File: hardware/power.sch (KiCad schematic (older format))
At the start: 18 parts, among them J7 Barrel_Jack, U18 LT1529CQ#PBF, U19 LT1528CQ

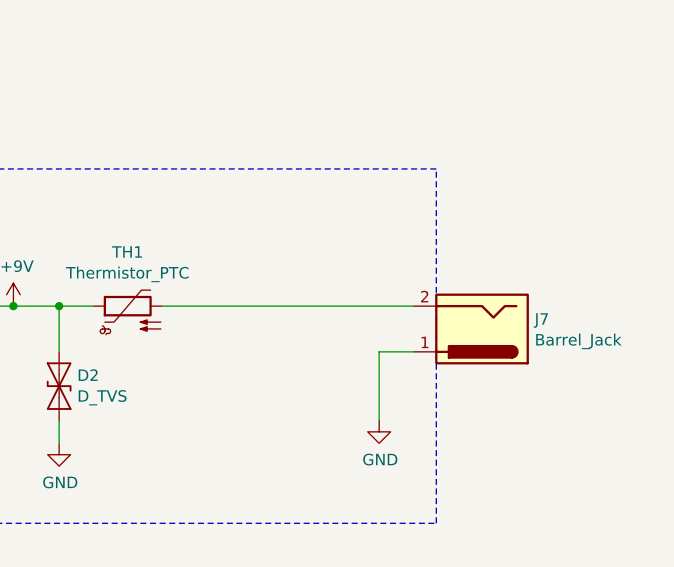
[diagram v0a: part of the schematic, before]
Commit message: update top overlay, drc przechodzi, dodny shielding wokół ścieżek zegarowych, dodane zdjęcia płytki
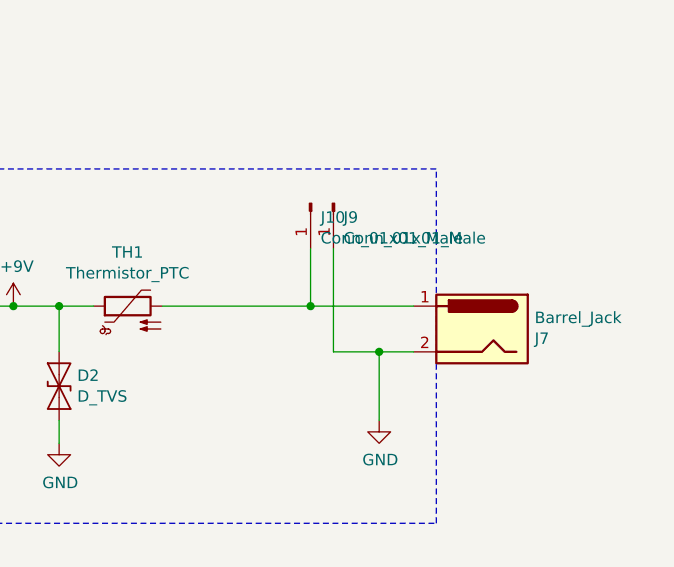
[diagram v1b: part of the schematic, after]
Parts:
- added J10, J9: Conn_01x01_Male, Connector_Wire:SolderWirePad_1x01_Drill2.5mm, symbol Connector:Conn_01x01_Male
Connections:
- net GND: now also J7.2, J9.1 (Pin_1); no longer J7.1
- net at TH1.2: now also J7.1, J10.1 (Pin_1); no longer J7.2
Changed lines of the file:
@@
 F 3 "~" H 10050 2010 50  0001 C CNN
 	1    10000 2050
-	-1   0    0    1
+	-1   0    0    -1
 $EndComp
 Wire Wire Line
@@
 	8150 1950 7950 1950
 Wire Wire Line
-	8600 1950 9700 1950
+	8600 1950 9250 1950
 Wire Wire Line
 	2650 4200 2650 4400
@@
 Wire Wire Line
 	7000 4250 7750 4250
+Wire Wire Line
+	9350 1700 9350 2150
+Wire Wire Line
+	9350 2150 9550 2150
+Connection ~ 9550 2150
+Wire Wire Line
+	9250 1700 9250 1950
+Connection ~ 9250 1950
+Wire Wire Line
+	9250 1950 9700 1950
+$Comp
+L Connector:Conn_01x01_Male J9
+U 1 1 5CF71EF7
+P 9350 1500
+F 0 "J9" V 9412 1544 50  0000 L CNN
+F 1 "Conn_01x01_Male" V 9503 1544 50  0000 L CNN
+F 2 "Connector_Wire:SolderWirePad_1x01_Drill2.5mm" H 9350 1500 50  0001 C CNN
+F 3 "~" H 9350 1500 50  0001 C CNN
+	1    9350 1500
+	0    1    1    0
+$EndComp
+$Comp
+L Connector:Conn_01x01_Male J10
+U 1 1 5CF74160
+P 9250 1500
+F 0 "J10" V 9312 1544 50  0000 L CNN
+F 1 "Conn_01x01_Male" V 9403 1544 50  0000 L CNN
+F 2 "Connector_Wire:SolderWirePad_1x01_Drill2.5mm" H 9250 1500 50  0001 C CNN
+F 3 "~" H 9250 1500 50  0001 C CNN
+	1    9250 1500
+	0    1    1    0
+$EndComp
 $EndSCHEMATC

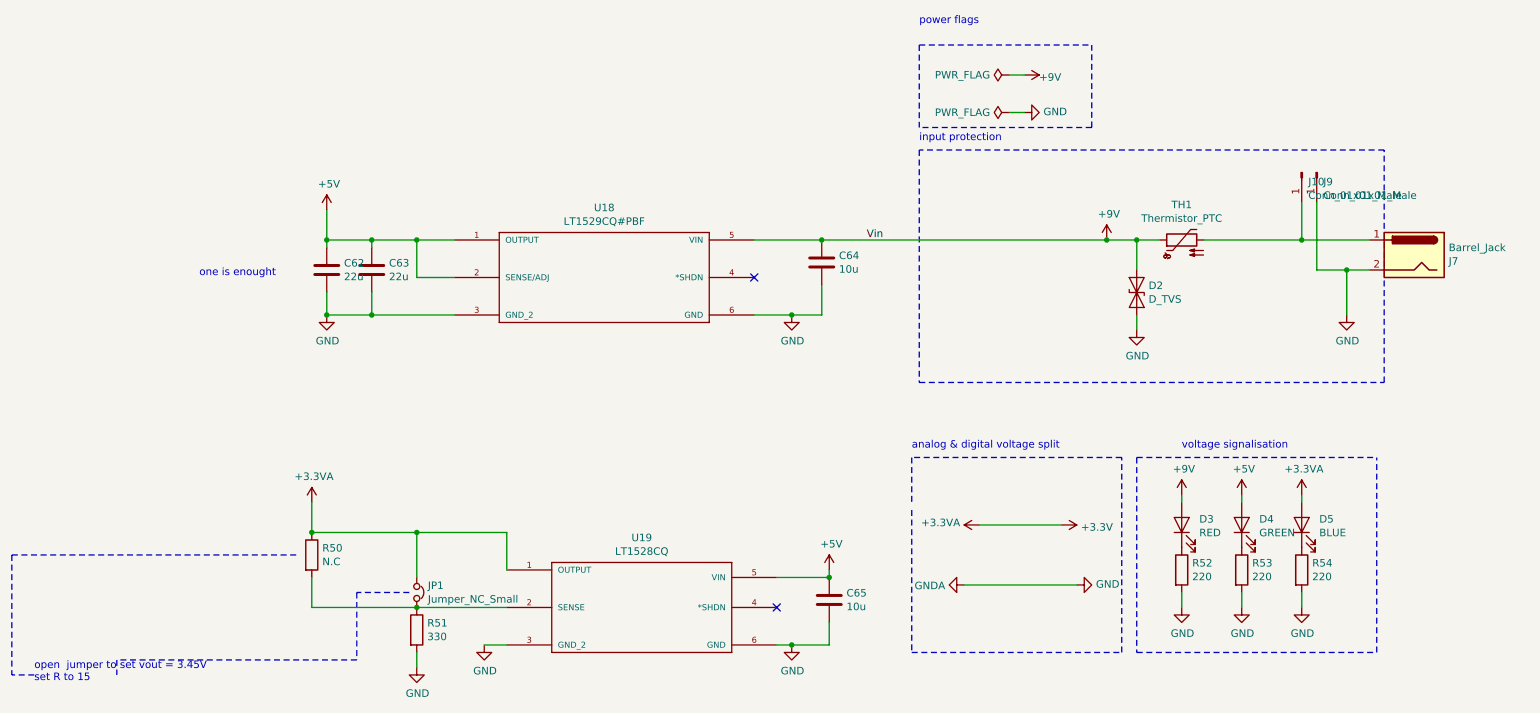
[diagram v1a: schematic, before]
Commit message: dodano poprawki błędów znalezionych podczas montażu
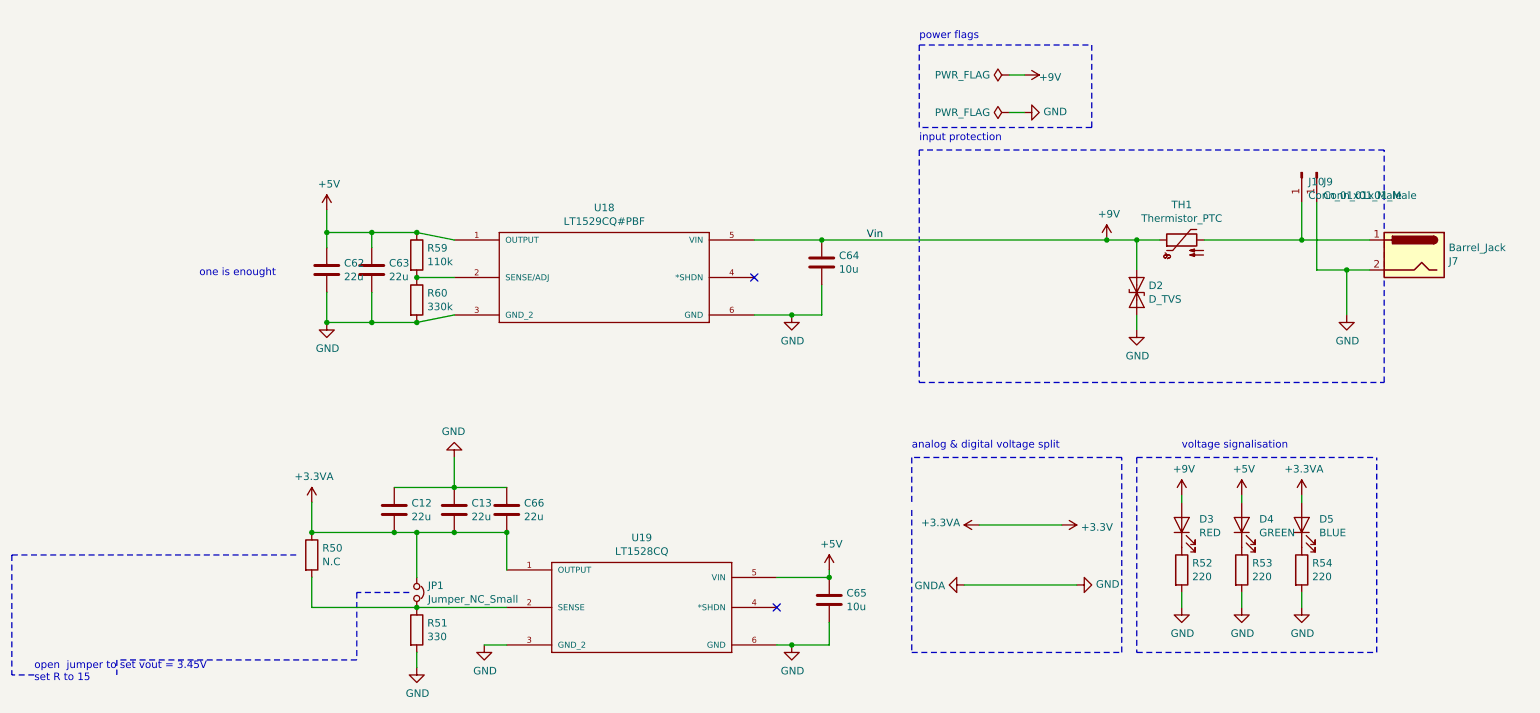
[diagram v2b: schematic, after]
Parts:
- added C12, C13, C66: 22u, Capacitor_SMD:C_0805_2012Metric_Pad1.15x1.40mm_HandSolder, symbol Device:C
- added R59: 110k, Resistor_SMD:R_0603_1608Metric_Pad1.05x0.95mm_HandSolder, symbol Device:R
- added R60: 330k, Resistor_SMD:R_0603_1608Metric_Pad1.05x0.95mm_HandSolder, symbol Device:R
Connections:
- net +3.3VA: now also C12.2, C13.2, C66.2
- net +5V: now also R59.1; no longer U18.2 (SENSE/ADJ)
- net GND: now also C12.1, C13.1, C66.1, R60.2
- new net: R59.2, R60.1, U18.2 (SENSE/ADJ)
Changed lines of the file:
@@
 	5850 4650 5750 4650
 Wire Wire Line
-	2650 4400 3350 4400
-Wire Wire Line
-	2650 3900 3350 3900
+	2650 3900 3200 3900
 Text Notes 800  4900 0    50   ~ 0
 open  jumper to set vout = 3.45V\nset R to 15
@@
 L power:GND #PWR0139
 U 1 1 5CEC8225
-P 2750 2450
-F 0 "#PWR0139" H 2750 2200 50  0001 C CNN
-F 1 "GND" H 2755 2277 50  0000 C CNN
-F 2 "" H 2750 2450 50  0001 C CNN
-F 3 "" H 2750 2450 50  0001 C CNN
-	1    2750 2450
-	1    0    0    -1
-$EndComp
-Wire Wire Line
-	3600 1950 3350 1950
-Wire Wire Line
-	3350 1950 3350 2200
+P 2750 2500
+F 0 "#PWR0139" H 2750 2250 50  0001 C CNN
+F 1 "GND" H 2755 2327 50  0000 C CNN
+F 2 "" H 2750 2500 50  0001 C CNN
+F 3 "" H 2750 2500 50  0001 C CNN
+	1    2750 2500
+	1    0    0    -1
+$EndComp
 Wire Wire Line
 	3350 2200 3600 2200
-Connection ~ 3350 1950
 $Comp
 L Device:C C62
@@
 $EndComp
 Wire Wire Line
-	3350 1950 3050 1950
-Wire Wire Line
-	2750 1950 2750 2000
-Wire Wire Line
-	2750 2300 2750 2450
-Connection ~ 2750 2450
-Wire Wire Line
-	2750 2450 3050 2450
+	2750 1900 2750 2000
+Wire Wire Line
+	2750 2300 2750 2500
+Connection ~ 2750 2500
+Wire Wire Line
+	2750 2500 3050 2500
 Wire Notes Line
 	3300 4300 2950 4300
@@
 $EndComp
 Wire Wire Line
-	3050 2000 3050 1950
-Connection ~ 3050 1950
-Wire Wire Line
-	3050 1950 2750 1950
-Wire Wire Line
-	3050 2300 3050 2450
-Connection ~ 3050 2450
-Wire Wire Line
-	3050 2450 3600 2450
+	3050 2000 3050 1900
+Connection ~ 3050 1900
+Wire Wire Line
+	3050 1900 2750 1900
+Wire Wire Line
+	3050 2300 3050 2500
+Connection ~ 3050 2500
+Wire Wire Line
+	3050 2500 3350 2500
 Text Notes 1900 2200 0    50   ~ 0
 one is enought\n
@@
 	3350 3900 3350 4200
 Wire Wire Line
-	3350 3900 3950 3900
+	3350 3900 3600 3900
 Wire Wire Line
 	3950 3900 3950 4150
@@
 $EndComp
 Wire Wire Line
-	2750 1750 2750 1950
-Connection ~ 2750 1950
+	2750 1750 2750 1900
+Connection ~ 2750 1900
 Wire Notes Line
 	6700 2900 9800 2900
@@
 	0    -1   -1   0
 $EndComp
-Text Notes 6700 600  0    50   ~ 0
+Text Notes 6700 700  0    50   ~ 0
 power flags\n\n
 Wire Notes Line
@@
 	0    1    1    0
 $EndComp
+Wire Wire Line
+	3050 1900 3350 1900
+$Comp
+L Device:R R59
+U 1 1 5D0518B3
+P 3350 2050
+F 0 "R59" H 3420 2096 50  0000 L CNN
+F 1 "110k" H 3420 2005 50  0000 L CNN
+F 2 "Resistor_SMD:R_0603_1608Metric_Pad1.05x0.95mm_HandSolder" V 3280 2050 50  0001 C CNN
+F 3 "~" H 3350 2050 50  0001 C CNN
+	1    3350 2050
+	1    0    0    -1
+$EndComp
+$Comp
+L Device:R R60
+U 1 1 5D052142
+P 3350 2350
+F 0 "R60" H 3420 2396 50  0000 L CNN
+F 1 "330k" H 3420 2305 50  0000 L CNN
+F 2 "Resistor_SMD:R_0603_1608Metric_Pad1.05x0.95mm_HandSolder" V 3280 2350 50  0001 C CNN
+F 3 "~" H 3350 2350 50  0001 C CNN
+	1    3350 2350
+	1    0    0    -1
+$EndComp
+Connection ~ 3350 2200
+Connection ~ 3350 1900
+Wire Wire Line
+	3350 1900 3600 1950
+Connection ~ 3350 2500
+Wire Wire Line
+	3350 2500 3600 2450
+$Comp
+L Device:C C12
+U 1 1 5D05AD55
+P 3200 3750
+F 0 "C12" H 3315 3796 50  0000 L CNN
+F 1 "22u" H 3315 3705 50  0000 L CNN
+F 2 "Capacitor_SMD:C_0805_2012Metric_Pad1.15x1.40mm_HandSolder" H 3238 3600 50  0001 C CNN
+F 3 "~" H 3200 3750 50  0001 C CNN
+	1    3200 3750
+	1    0    0    -1
+$EndComp
+Wire Wire Line
+	2650 4400 3350 4400
+$Comp
+L Device:C C13
+U 1 1 5D0611C8
+P 3600 3750
+F 0 "C13" H 3715 3796 50  0000 L CNN
+F 1 "22u" H 3715 3705 50  0000 L CNN
+F 2 "Capacitor_SMD:C_0805_2012Metric_Pad1.15x1.40mm_HandSolder" H 3638 3600 50  0001 C CNN
+F 3 "~" H 3600 3750 50  0001 C CNN
+	1    3600 3750
+	1    0    0    -1
+$EndComp
+$Comp
+L Device:C C66
+U 1 1 5D061541
+P 3950 3750
+F 0 "C66" H 4065 3796 50  0000 L CNN
+F 1 "22u" H 4065 3705 50  0000 L CNN
+F 2 "Capacitor_SMD:C_0805_2012Metric_Pad1.15x1.40mm_HandSolder" H 3988 3600 50  0001 C CNN
+F 3 "~" H 3950 3750 50  0001 C CNN
+	1    3950 3750
+	1    0    0    -1
+$EndComp
+Connection ~ 3950 3900
+Connection ~ 3200 3900
+Wire Wire Line
+	3200 3900 3350 3900
+Connection ~ 3600 3900
+Wire Wire Line
+	3600 3900 3950 3900
+$Comp
+L power:GND #PWR0149
+U 1 1 5D061BB4
+P 3600 3400
+F 0 "#PWR0149" H 3600 3150 50  0001 C CNN
+F 1 "GND" H 3605 3227 50  0000 C CNN
+F 2 "" H 3600 3400 50  0001 C CNN
+F 3 "" H 3600 3400 50  0001 C CNN
+	1    3600 3400
+	-1   0    0    1
+$EndComp
+Wire Wire Line
+	3200 3600 3600 3600
+Connection ~ 3600 3600
+Wire Wire Line
+	3600 3600 3950 3600
+Wire Wire Line
+	3600 3600 3600 3400
 $EndSCHEMATC
